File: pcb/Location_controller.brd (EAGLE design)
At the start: 75 x 48 mm, 62 parts, among them IC1 LIS302DL

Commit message: Move powerpins
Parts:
- moved PWR 12.2 mm to (64.5, 45.4), turned to 180 degrees
- moved R7 9.84 mm to (69.8, 45.4), turned to 0 degrees
- moved RCM_POWER 3.56 mm to (68.1, 38.6)
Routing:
- net VDD: track 274.9 -> 290.8 mm
- net GND: track 294.1 -> 284.7 mm
- net IN_3V: track 39.4 -> 35.6 mm
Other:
- board text added: "HOP 05: Drone V 1.0 - 21/03/2014"
- board text removed: "HOP 05 V 1.0"
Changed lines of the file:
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@@
 <text x="15.75" y="37.11" size="1.778" layer="25">SCL</text>
 <circle x="73.38" y="3.44" radius="0.45276875" width="0.4064" layer="25"/>
-<text x="11.14" y="12.44" size="1.778" layer="25" rot="R180">HOP 05
-V 1.0</text>
+<text x="18.11" y="11.07" size="1.4224" layer="25" rot="R180">HOP 05: Drone
+V 1.0 - 21/03/2014</text>
 </plain>
 <attributes>
@@
 <attribute name="VALUE" x="6.935" y="38.15" size="1.27" layer="27" rot="R90"/>
 </element>
-<element name="RCM_POWER" library="pinhead" package="1X02" value="" x="71.14" y="40.35" smashed="yes" rot="R90">
-<attribute name="NAME" x="74.2762" y="44.6012" size="1.27" layer="25" ratio="10" rot="R180"/>
-<attribute name="VALUE" x="74.315" y="37.81" size="1.27" layer="27" rot="R90"/>
+<element name="RCM_POWER" library="pinhead" package="1X02" value="" x="68.06" y="38.57" smashed="yes" rot="R90">
+<attribute name="NAME" x="71.8488" y="43.2562" size="1.27" layer="25" ratio="10" rot="R270"/>
+<attribute name="VALUE" x="71.235" y="36.03" size="1.27" layer="27" rot="R90"/>
 </element>
 <element name="U$2" library="adafruit" package="PJ-102A" value="2.1MMJACKTHM" x="70.62" y="26.92" rot="R270"/>
@@
 <element name="JP2" library="pinhead" package="1X06" value="" x="25.4" y="2.54"/>
 <element name="JP3" library="pinhead" package="1X06" value="" x="8.89" y="2.54"/>
-<element name="PWR" library="eagle-ltspice" package="LED_1206" value="" x="70.27" y="34.72" smashed="yes" rot="R270">
-<attribute name="SPICEMODEL" value="NONE" x="70.27" y="34.72" size="1.778" layer="27" rot="R270" display="off"/>
-<attribute name="SPICETYPE" value="diode" x="70.27" y="34.72" size="1.778" layer="27" rot="R270" display="off"/>
-<attribute name="SPICEPREFIX" value="D" x="70.27" y="34.72" size="1.778" layer="27" rot="R270" display="off"/>
-<attribute name="NAME" x="71.44" y="36.66" size="1.27" layer="25" rot="R270"/>
-<attribute name="VALUE" x="67.73" y="35.99" size="1.27" layer="27" rot="R270"/>
-</element>
-<element name="R7" library="eagle-ltspice" package="R0805" value="68" x="66.46" y="36.16" rot="R180">
-<attribute name="SPICEMODEL" value="NONE" x="66.46" y="36.16" size="1.778" layer="27" rot="R180" display="off"/>
-<attribute name="SPICEPREFIX" value="R" x="66.46" y="36.16" size="1.778" layer="27" rot="R180" display="off"/>
+<element name="PWR" library="eagle-ltspice" package="LED_1206" value="" x="64.47" y="45.43" smashed="yes" rot="R180">
+<attribute name="SPICEMODEL" value="NONE" x="64.47" y="45.43" size="1.778" layer="27" rot="R180" display="off"/>
+<attribute name="SPICETYPE" value="diode" x="64.47" y="45.43" size="1.778" layer="27" rot="R180" display="off"/>
+<attribute name="SPICEPREFIX" value="D" x="64.47" y="45.43" size="1.778" layer="27" rot="R180" display="off"/>
+<attribute name="NAME" x="66.01" y="44.45" size="1.27" layer="25" rot="R180"/>
+<attribute name="VALUE" x="65.74" y="47.97" size="1.27" layer="27" rot="R180"/>
+</element>
+<element name="R7" library="eagle-ltspice" package="R0805" value="68" x="69.79" y="45.42" smashed="yes">
+<attribute name="SPICEMODEL" value="NONE" x="69.79" y="45.42" size="1.778" layer="27" display="off"/>
+<attribute name="SPICEPREFIX" value="R" x="69.79" y="45.42" size="1.778" layer="27" display="off"/>
+<attribute name="NAME" x="71.735" y="44.35" size="1.27" layer="25"/>
+<attribute name="VALUE" x="69.155" y="42.88" size="1.27" layer="27"/>
 </element>
 <element name="R8" library="eagle-ltspice" package="R0805" value="68" x="54.41" y="17.98" smashed="yes" rot="R180">
@@
 <wire x1="73.32" y1="8.58" x2="73.52" y2="8.78" width="0.4064" layer="16"/>
 <wire x1="73.52" y1="8.78" x2="73.52" y2="36.7" width="1.6764" layer="16"/>
-<wire x1="73.52" y1="36.7" x2="71.14" y2="39.08" width="1.6764" layer="16"/>
 <wire x1="52.26" y1="32.22" x2="51.35" y2="32.22" width="0.4064" layer="1"/>
 <wire x1="51.35" y1="32.22" x2="50.04" y2="33.53" width="0.4064" layer="1"/>
@@
 <wire x1="33.67" y1="32.25" x2="34.87" y2="31.05" width="0.4064" layer="16"/>
 <wire x1="34.87" y1="31.05" x2="36.81" y2="31.05" width="0.4064" layer="16"/>
-<wire x1="70.27" y1="33.298" x2="70.442" y2="33.47" width="1.016" layer="1"/>
 <contactref element="D4" pad="2"/>
 <contactref element="D3" pad="2"/>
@@
 <wire x1="59.32" y1="42.24" x2="55.69" y2="38.61" width="1.27" layer="1"/>
 <wire x1="65.41" y1="42.24" x2="65.41" y2="38.73" width="1.27" layer="1"/>
-<wire x1="71.14" y1="39.08" x2="65.41" y2="39.08" width="1.27" layer="1"/>
 <wire x1="65.41" y1="39.08" x2="65.41" y2="38.73" width="1.27" layer="1"/>
 <contactref element="D6" pad="A"/>
@@
 <wire x1="63.21" y1="38.71" x2="60.78" y2="38.71" width="0.4064" layer="1"/>
 <wire x1="55.68" y1="34.1" x2="62.72" y2="34.1" width="0.4064" layer="1"/>
-<wire x1="62.72" y1="34.1" x2="63.54" y2="34.92" width="0.4064" layer="1"/>
-<wire x1="63.51" y1="38.73" x2="63.51" y2="36.16" width="0.4064" layer="1"/>
-<wire x1="63.51" y1="36.16" x2="63.51" y2="34.95" width="0.4064" layer="1"/>
+<wire x1="62.72" y1="34.1" x2="63.425" y2="34.805" width="0.4064" layer="1"/>
+<wire x1="63.425" y1="34.805" x2="63.54" y2="34.92" width="0.4064" layer="1"/>
+<wire x1="63.51" y1="38.73" x2="63.51" y2="34.95" width="0.4064" layer="1"/>
 <wire x1="63.51" y1="34.95" x2="63.54" y2="34.92" width="0.4064" layer="1"/>
 <wire x1="51.03" y1="30.55" x2="50.32" y2="31.26" width="0.4064" layer="1"/>
@@
 <wire x1="56.86" y1="3.35" x2="56.86" y2="10.27" width="0.4064" layer="1"/>
 <contactref element="R7" pad="2"/>
-<wire x1="65.51" y1="36.16" x2="63.51" y2="36.16" width="0.4064" layer="1"/>
 <contactref element="R5" pad="1"/>
 <wire x1="36.58" y1="35.96" x2="36.58" y2="37.62" width="0.4064" layer="1"/>
@@
 <wire x1="28.26" y1="27.14" x2="28.26" y2="27.42" width="0.3048" layer="1"/>
 <wire x1="28.26" y1="27.42" x2="27.34" y2="28.34" width="0.3048" layer="1"/>
+<wire x1="70.74" y1="45.42" x2="70.74" y2="35.14" width="0.4064" layer="1"/>
+<wire x1="70.74" y1="35.14" x2="70.19" y2="34.59" width="0.4064" layer="1"/>
+<wire x1="70.19" y1="34.59" x2="63.64" y2="34.59" width="0.4064" layer="1"/>
+<wire x1="63.64" y1="34.59" x2="63.425" y2="34.805" width="0.4064" layer="1"/>
 </signal>
 <signal name="I2C_SCL">
@@
 <wire x1="55.69" y1="36.72" x2="55.69" y2="36.71" width="0.4064" layer="1"/>
 <contactref element="RCM_POWER" pad="2"/>
-<wire x1="71.14" y1="41.62" x2="63.95" y2="41.62" width="1.6764" layer="16"/>
-<wire x1="63.95" y1="41.62" x2="59.45" y2="37.12" width="1.6764" layer="16"/>
-<wire x1="59.45" y1="37.12" x2="53.56" y2="37.12" width="1.6764" layer="16"/>
+<wire x1="61.28" y1="37.12" x2="53.56" y2="37.12" width="1.6764" layer="16"/>
 <wire x1="53.56" y1="37.12" x2="51.97" y2="38.71" width="1.6764" layer="16"/>
 <wire x1="51.97" y1="38.71" x2="51.97" y2="41.38" width="1.6764" layer="16"/>
 <wire x1="51.97" y1="41.38" x2="51.92" y2="41.43" width="0.4064" layer="16"/>
+<wire x1="68.06" y1="39.84" x2="64" y2="39.84" width="1.6764" layer="16"/>
+<wire x1="64" y1="39.84" x2="61.28" y2="37.12" width="1.6764" layer="16"/>
 </signal>
 <signal name="N$4">
@@
 <contactref element="PWR" pad="A"/>
 <contactref element="R7" pad="1"/>
-<wire x1="67.41" y1="36.16" x2="70.27" y2="36.16" width="0.4064" layer="1"/>
-<wire x1="70.27" y1="36.16" x2="70.27" y2="36.142" width="0.4064" layer="1"/>
+<wire x1="68.84" y1="45.42" x2="65.902" y2="45.42" width="0.4064" layer="1"/>
+<wire x1="65.902" y1="45.42" x2="65.892" y2="45.43" width="0.4064" layer="1"/>
 </signal>
 <signal name="N$13">

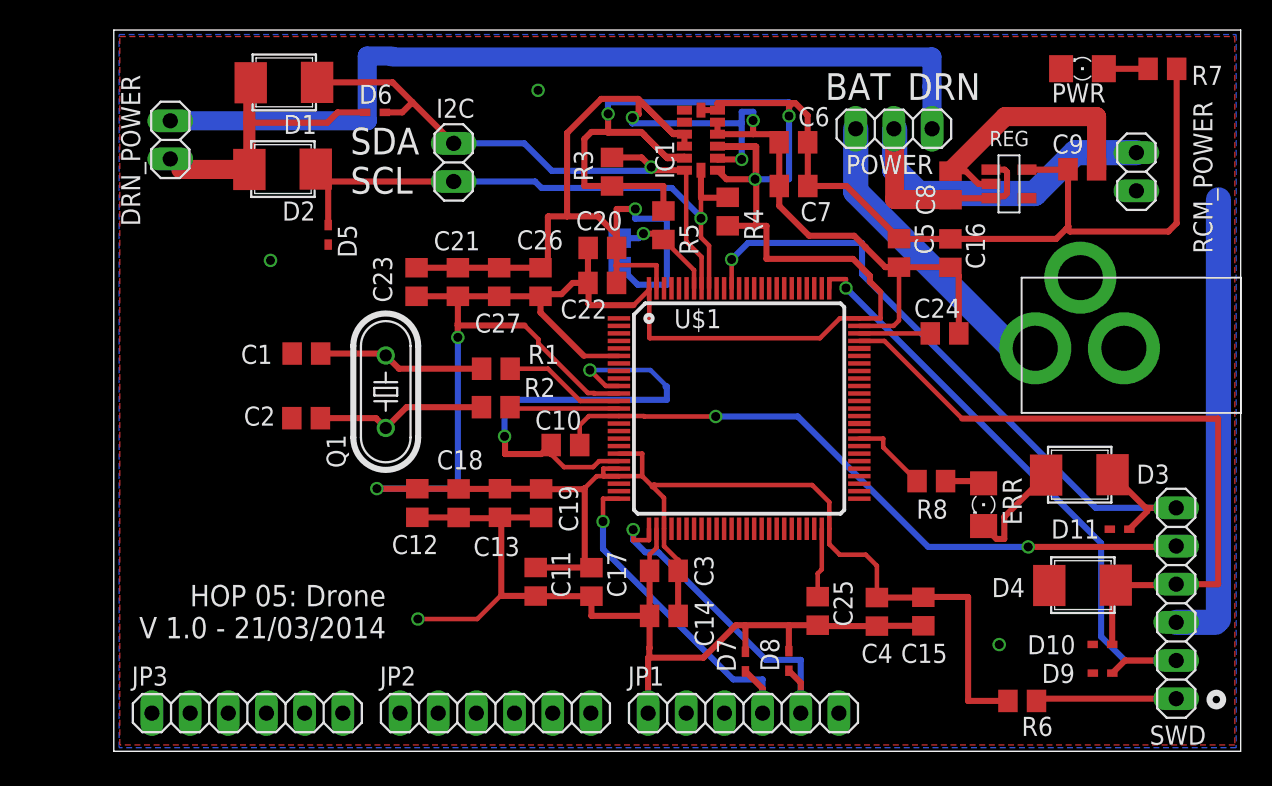
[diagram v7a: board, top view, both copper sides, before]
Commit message: Move RCM_POWER pins to correct position
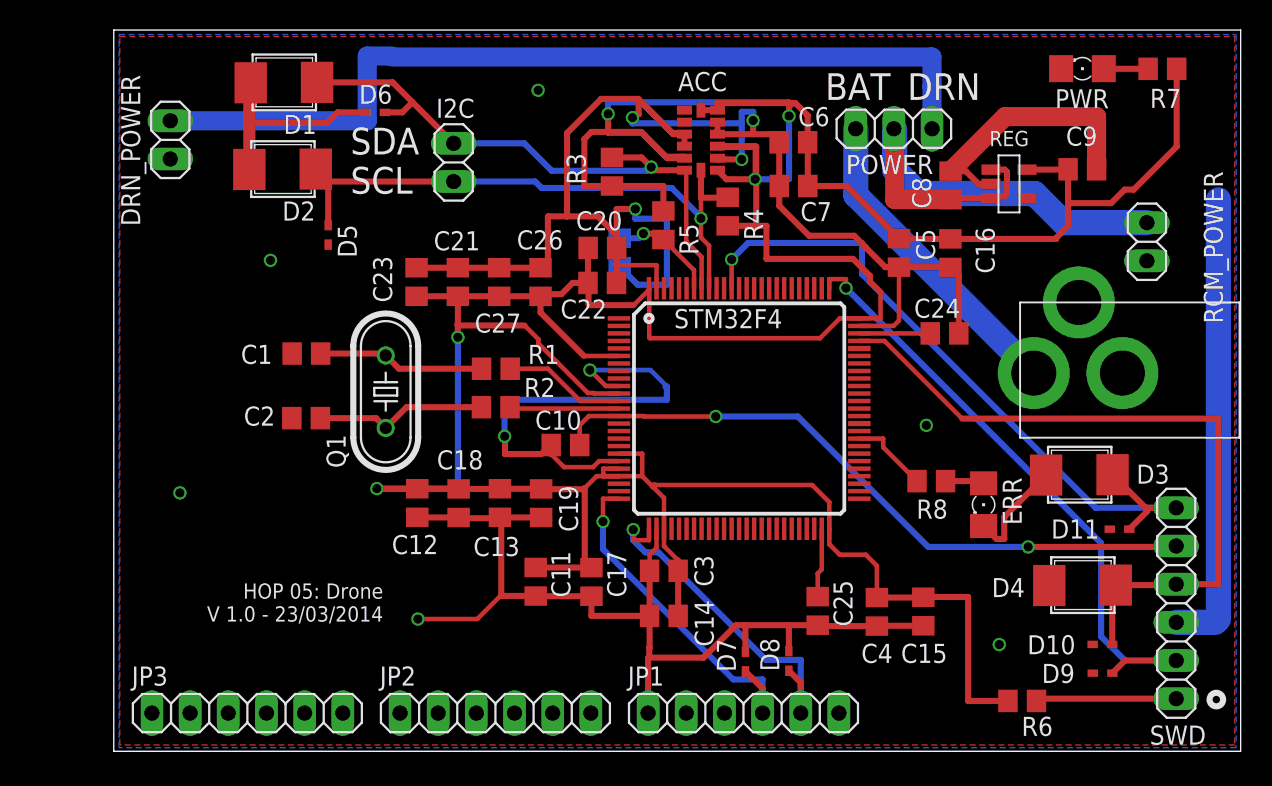
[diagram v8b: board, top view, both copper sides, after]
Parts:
- moved RCM_POWER 4.71 mm to (68.8, 33.9)
- moved U$2 1.65 mm to (70.5, 25.3)
- renumbered IC1 to ACC, U$1 to STM32F4
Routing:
- net GND: track 284.7 -> 279.1 mm, vias 10 -> 12
- net VDD: track 290.8 -> 286.9 mm
- net N$5: track 20.5 -> 21.2 mm
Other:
- board text added: "HOP 05: Drone V 1.0 - 23/03/2014"
- board text removed: "HOP 05: Drone V 1.0 - 21/03/2014"
